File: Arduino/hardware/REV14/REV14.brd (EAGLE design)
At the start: 100 x 50 mm, 57 parts, among them IC1 LTC3525, IC2 ATMEGA168-AU, IC3 TS1003IG5TMF, Q1 32768Hz, U1 RN2483, U2 TMP112

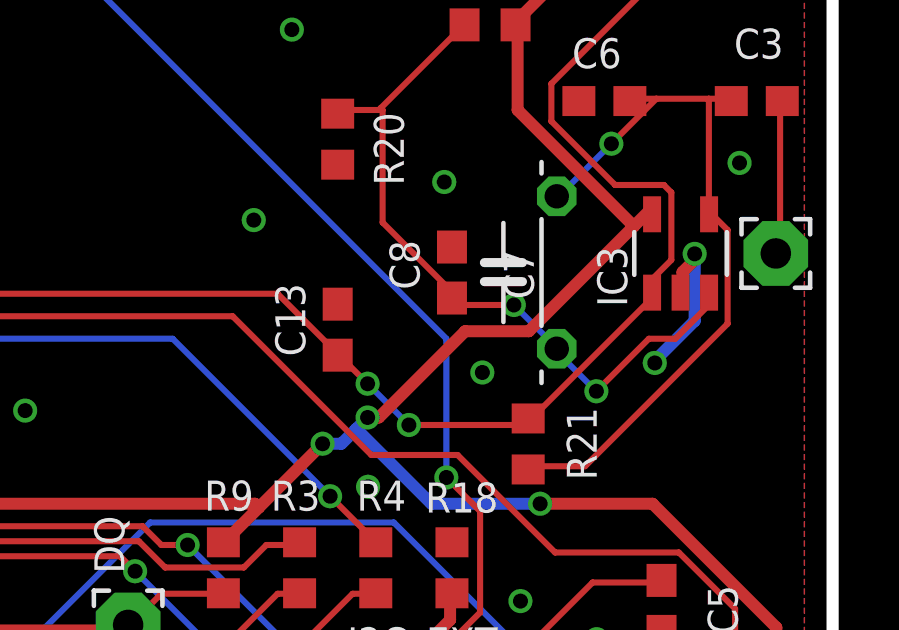
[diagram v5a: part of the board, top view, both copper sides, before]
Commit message: fixed cap footprint for mobile detect
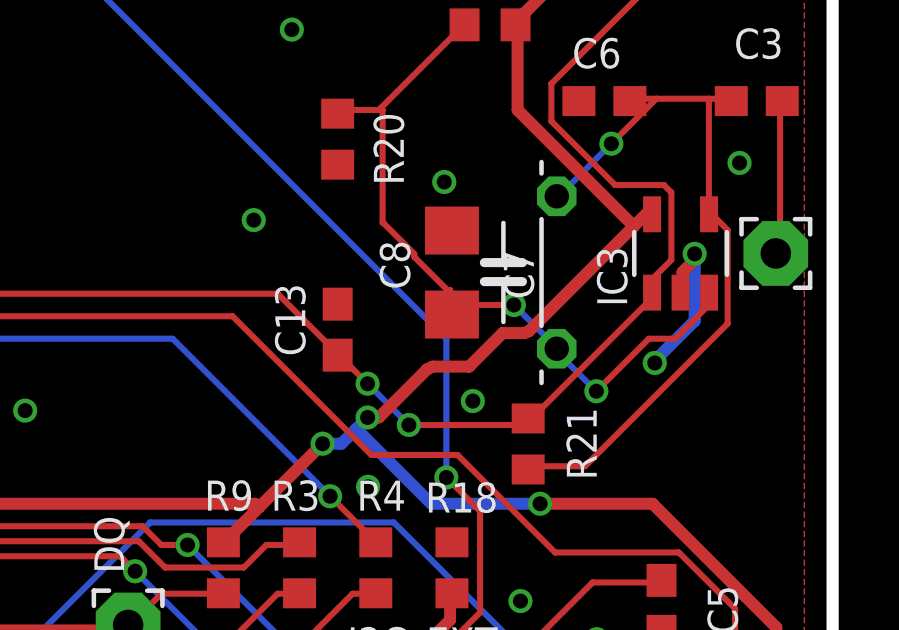
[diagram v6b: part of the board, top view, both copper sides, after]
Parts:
- C8: device resistor:C0603 -> rcl:C1206
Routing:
- net N$21: track 24.4 -> 25.3 mm
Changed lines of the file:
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@@
 <attribute name="NAME" x="90.043" y="24.1935" size="1" layer="25" rot="R90"/>
 </element>
-<element name="C8" library="resistor" package="C0603" value="100uF" x="87.3125" y="25.0825" smashed="yes" rot="R90">
-<attribute name="NAME" x="86.233" y="24.511" size="1" layer="25" rot="R90"/>
+<element name="C8" library="rcl" package="C1206" value="100uF" x="87.3125" y="25.0825" smashed="yes" rot="R90">
+<attribute name="NAME" x="85.9155" y="24.511" size="1" layer="25" rot="R90"/>
 </element>
 <element name="R19" library="resistor" package="R0603" value="2.2M" x="88.5825" y="33.3375" smashed="yes" rot="R180">
@@
 <via x="62.925" y="11.9075" extent="1-16" drill="0.5"/>
 <via x="92.135" y="12.86" extent="1-16" drill="0.5"/>
-<via x="88.325" y="21.75" extent="1-16" drill="0.5"/>
+<via x="88.0075" y="20.7975" extent="1-16" drill="0.5"/>
 <via x="96.8975" y="28.735" extent="1-16" drill="0.5"/>
 </signal>
@@
 <wire x1="84.125" y1="19.875" x2="83.625" y2="19.375" width="0.4" layer="16"/>
 <wire x1="84.875" y1="20.25" x2="84.5" y2="20.25" width="0.4" layer="1"/>
-<wire x1="87.75" y1="23.125" x2="84.875" y2="20.25" width="0.4" layer="1"/>
-<wire x1="89.875" y1="23.125" x2="87.75" y2="23.125" width="0.4" layer="1"/>
+<wire x1="86.48" y1="21.855" x2="84.875" y2="20.25" width="0.4" layer="1"/>
 <wire x1="93.875" y1="27.125" x2="93.375" y2="26.625" width="0.4" layer="1"/>
 <wire x1="93.375" y1="26.625" x2="89.875" y2="23.125" width="0.4" layer="1"/>
@@
 <via x="68" y="14.875" extent="1-16" drill="0.5"/>
 <via x="70.5" y="17.375" extent="1-16" drill="0.5"/>
+<wire x1="89.0016" y1="23.0632" x2="89.7128" y2="23.0632" width="0.4" layer="1"/>
+<wire x1="87.884" y1="21.9456" x2="89.0016" y2="23.0632" width="0.4" layer="1"/>
+<wire x1="86.6648" y1="21.9456" x2="87.884" y2="21.9456" width="0.4" layer="1"/>
+<wire x1="89.7128" y1="23.0632" x2="89.875" y2="23.125" width="0.4" layer="1"/>
+<wire x1="86.6648" y1="21.9456" x2="86.48" y2="21.855" width="0.4" layer="1"/>
 </signal>
 <signal name="SPI_SCK">
@@
 <wire x1="83.625" y1="30.5" x2="83.5025" y2="30.3775" width="0.2032" layer="1"/>
 <wire x1="87.625" y1="33.25" x2="87.7325" y2="33.3375" width="0.2032" layer="1"/>
-<wire x1="87.25" y1="24.5" x2="87.25" y2="24.25" width="0.2032" layer="1"/>
-<wire x1="85" y1="26.75" x2="87.25" y2="24.5" width="0.2032" layer="1"/>
+<wire x1="87.25" y1="24.5" x2="87.25" y2="24.4856" width="0.2032" layer="1"/>
+<wire x1="87.25" y1="24.4856" x2="87.25" y2="24.25" width="0.2032" layer="1"/>
 <wire x1="85" y1="30.5" x2="85" y2="26.75" width="0.2032" layer="1"/>
-<wire x1="87.25" y1="24.25" x2="87.3125" y2="24.2325" width="0.2032" layer="1"/>
+<wire x1="87.25" y1="24.25" x2="87.3125" y2="23.6825" width="0.2032" layer="1"/>
 <wire x1="85" y1="30.5" x2="84.9375" y2="30.5625" width="0.2032" layer="1"/>
 <wire x1="89.375" y1="24" x2="90.75" y2="22.625" width="0.2032" layer="16"/>
@@
 <wire x1="87.375" y1="24.125" x2="87.5" y2="24" width="0.2032" layer="1"/>
 <wire x1="90.75" y1="22.625" x2="90.805" y2="22.5425" width="0.2032" layer="16"/>
-<wire x1="87.375" y1="24.125" x2="87.3125" y2="24.2325" width="0.2032" layer="1"/>
+<wire x1="87.375" y1="24.125" x2="87.3125" y2="23.6825" width="0.2032" layer="1"/>
 <via x="92.125" y="21.125" extent="1-16" drill="0.5"/>
 <via x="89.375" y="24" extent="1-16" drill="0.5"/>
+<wire x1="86.0552" y1="25.7048" x2="85.0392" y2="26.7208" width="0.2032" layer="1"/>
+<wire x1="86.0552" y1="25.6032" x2="86.0552" y2="25.7048" width="0.2032" layer="1"/>
+<wire x1="87.1728" y1="24.4856" x2="86.0552" y2="25.6032" width="0.2032" layer="1"/>
+<wire x1="85.0392" y1="26.7208" x2="85" y2="26.75" width="0.2032" layer="1"/>
+<wire x1="87.1728" y1="24.4856" x2="87.25" y2="24.4856" width="0.2032" layer="1"/>
 </signal>
 </signals>

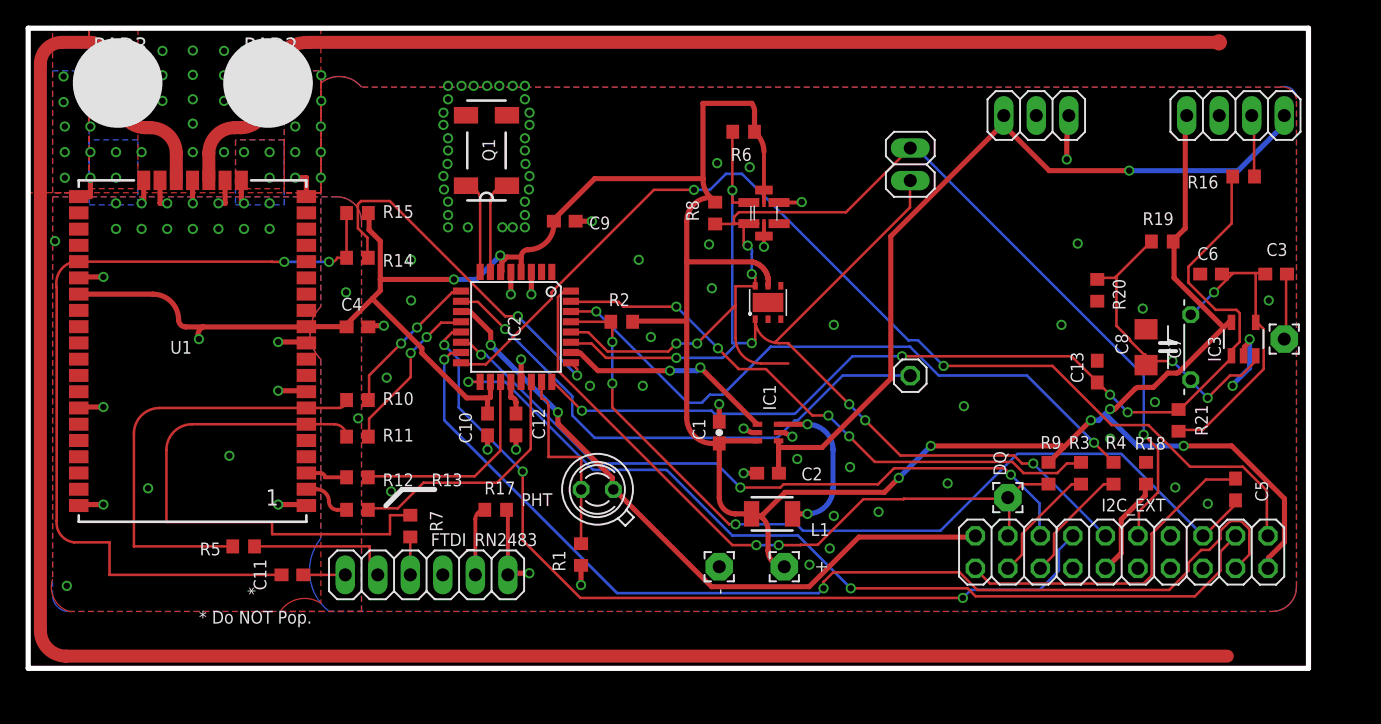
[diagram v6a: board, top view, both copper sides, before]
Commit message: added more stitching to rev14
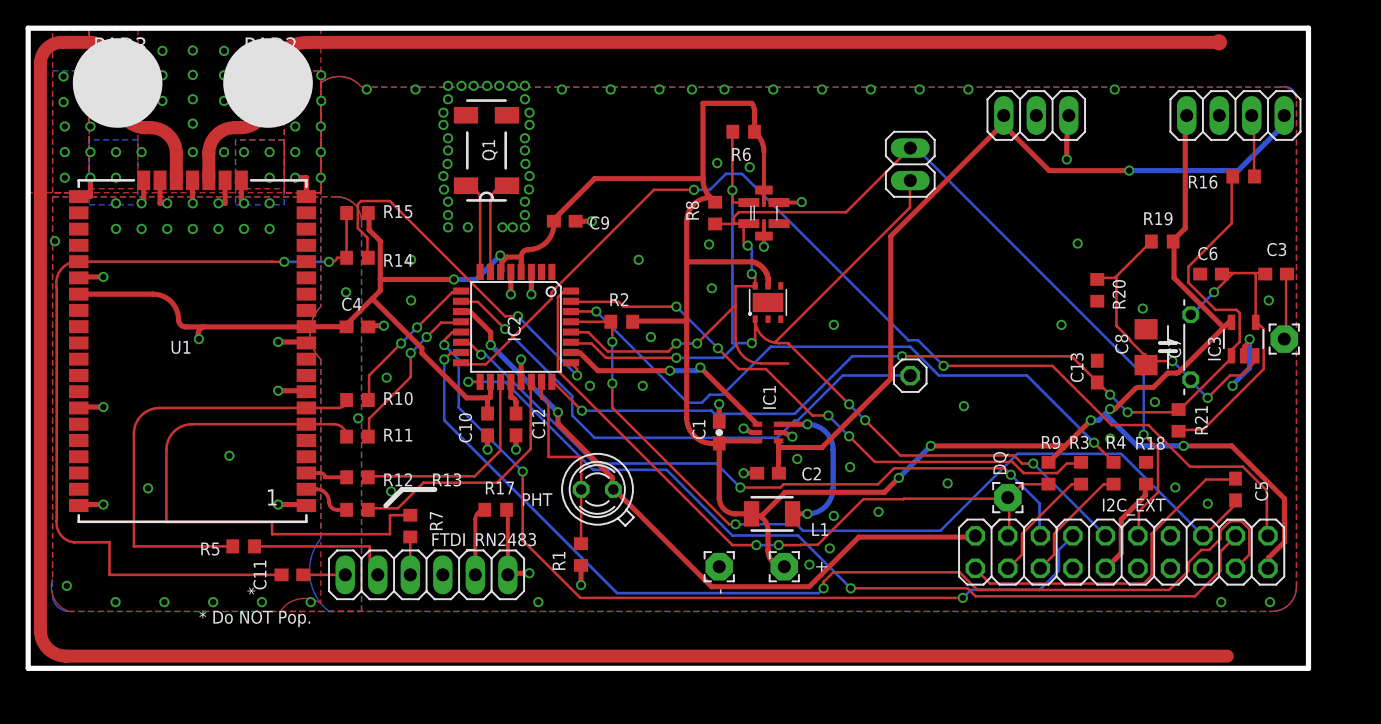
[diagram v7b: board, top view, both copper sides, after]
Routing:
- net GND: vias 141 -> 162
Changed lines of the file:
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@@
 <via x="88.0075" y="20.7975" extent="1-16" drill="0.5"/>
 <via x="96.8975" y="28.735" extent="1-16" drill="0.5"/>
+<via x="26.445" y="45.2125" extent="1-16" drill="0.5"/>
+<via x="30.255" y="45.2125" extent="1-16" drill="0.5"/>
+<via x="41.685" y="45.2125" extent="1-16" drill="0.5"/>
+<via x="45.495" y="45.2125" extent="1-16" drill="0.5"/>
+<via x="49.305" y="45.2125" extent="1-16" drill="0.5"/>
+<via x="51.845" y="45.2125" extent="1-16" drill="0.5"/>
+<via x="54.385" y="45.2125" extent="1-16" drill="0.5"/>
+<via x="58.195" y="45.2125" extent="1-16" drill="0.5"/>
+<via x="62.005" y="45.2125" extent="1-16" drill="0.5"/>
+<via x="65.815" y="45.2125" extent="1-16" drill="0.5"/>
+<via x="69.625" y="45.2125" extent="1-16" drill="0.5"/>
+<via x="73.435" y="45.2125" extent="1-16" drill="0.5"/>
+<via x="84.865" y="45.2125" extent="1-16" drill="0.5"/>
+<via x="6.825" y="5.1725" extent="1-16" drill="0.5"/>
+<via x="10.635" y="5.1725" extent="1-16" drill="0.5"/>
+<via x="14.445" y="5.1725" extent="1-16" drill="0.5"/>
+<via x="18.255" y="5.1725" extent="1-16" drill="0.5"/>
+<via x="22.065" y="5.1725" extent="1-16" drill="0.5"/>
+<via x="39.845" y="5.1725" extent="1-16" drill="0.5"/>
+<via x="96.995" y="5.1725" extent="1-16" drill="0.5"/>
+<via x="93.185" y="5.1725" extent="1-16" drill="0.5"/>
 </signal>
 <signal name="VCC" class="1">

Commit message: rev14 cut2
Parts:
- removed JP1: (no value), pinhead:1X01
- added U$1: (no value), ohw-logo:OSHW_10X200_NOTEXT
- JP2: device pinhead:1X02 -> pinhead:1X10
- JP3: device pinhead:1X03 -> pinhead:1X06
- PAD2, PAD3: device wirepad:3,81/1,4 -> wirepad:2,15/1,0
- moved JP2 10.7 mm to (72.4, 29.2)
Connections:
- net RN2483_UART_RX: now also R7.1; no longer R5.1
- net RN2483_UART_TX: now also R5.1; no longer R7.1
- net VOICE_NIRQ: now also JP2.8; no longer JP1.1
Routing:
- net VOICE_NIRQ: track 42.4 -> 85.8 mm
- net RN2483_UART_RX: track 34.2 -> 15.2 mm, vias 0 -> 2
- net SDA: track 88.4 -> 72.7 mm
- net RN2483_UART_TX: track 42.4 -> 26.9 mm, vias 0 -> 2
- net TX: track 50.9 -> 56.0 mm
- net SCL: track 90.0 -> 85.5 mm, vias 5 -> 6
- net GND: track 64.7 -> 67.3 mm, vias 162 -> 163
- net VCC1: track 64.1 -> 65.9 mm
- net PHONE: track 78.2 -> 80.0 mm
- net VCC: track 236.5 -> 238.0 mm
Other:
- board text added: "28/01-2016"
- board text added: "License: http://goo.gl/3d71UJ"
- board text added: "OpenTRV.org.uk"
- board text added: "REV14 Cut2"
